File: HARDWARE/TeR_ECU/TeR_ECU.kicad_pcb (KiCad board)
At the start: 4 copper layers, 108.5 x 67.8 mm, 167 parts, among them IC1 MX34040NF2, J1 RJ45_Shielded, J2 RJ45_Shielded, J3 DEBUG, J4 USB_B_Mini, J5 GPS_ANT, K2 G5Q-1, Q1 ZXMN3F30FH, Q2 ZXMN3F30FH, Q3 ZXMN3F30FH, Q4 ZXMN3F30FH, Q5 ZXMN3F30FH, SW1 RST, SW2 BOOT0, U1 TCAN332, U10 NEO-M9N, U11 AT24CS02-STUM, U2 TCAN332, U3 TSR_1-2450, U4 LM1117MP-3.3, U5 LM324, U6 STM32F405VGTx, U7 USBLC6-2SC6, U8 ASM330LHH, U9 LIS3MDL, Y2 ECS-250-20-33-CKM-TR

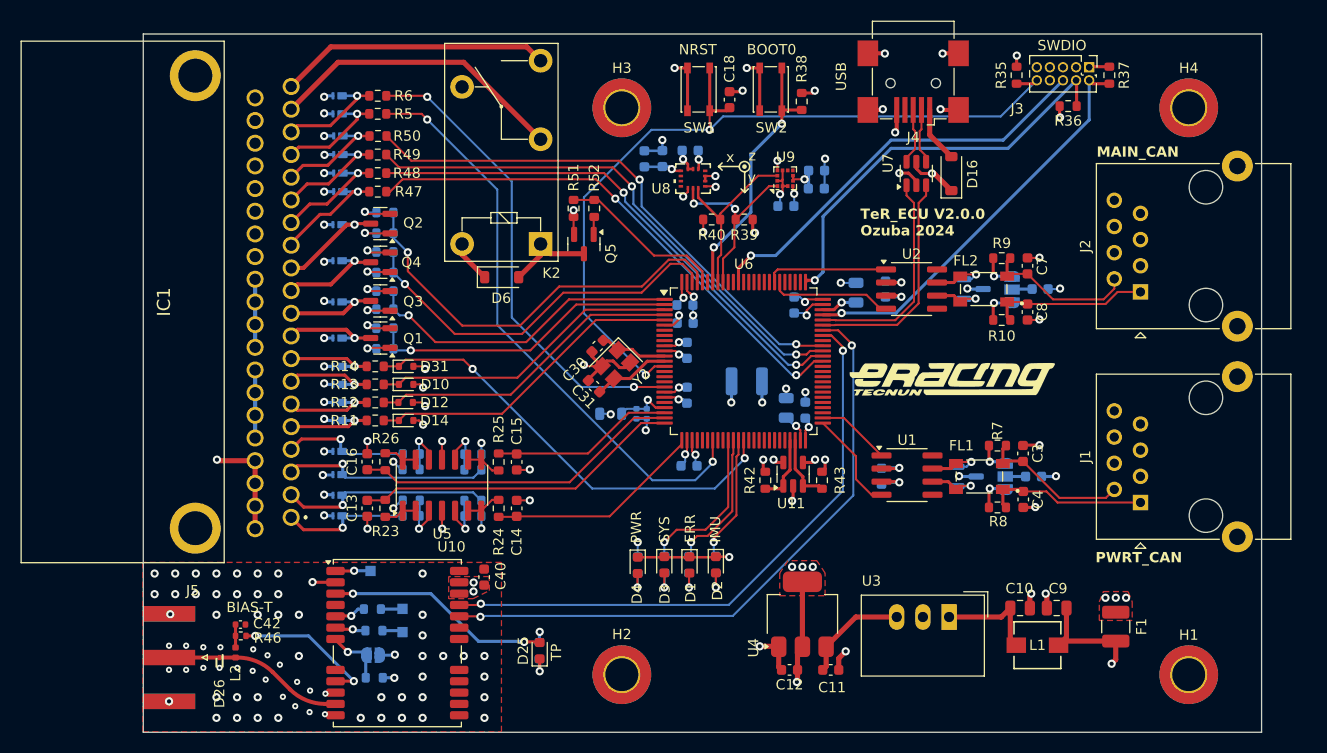
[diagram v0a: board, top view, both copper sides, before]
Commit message: Corregidos conectores, CAN y añadidas librerias al proyecto para cargar huellas
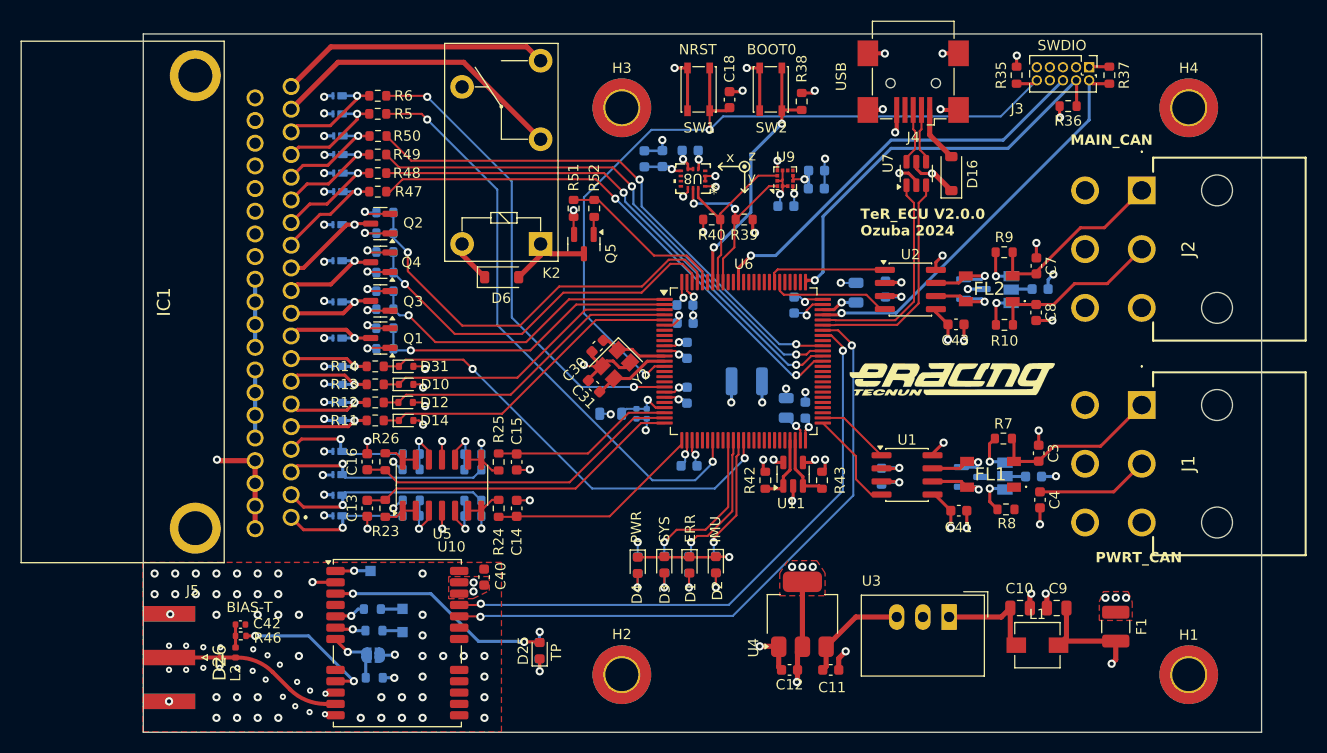
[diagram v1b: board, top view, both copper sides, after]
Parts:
- added C41: 100n, Capacitor_SMD:C_0603_1608Metric, F.Cu at (171.4, 104.8)
- added C43: 100n, Capacitor_SMD:C_0603_1608Metric, F.Cu at (171.1, 86.7)
- D26: footprint GPS_D:SODFL1006X40N -> ESD9101:SODFL1006X40N
- FL1, FL2: footprint CAN_CMF:FIL_ACT45B-510-2P-TL003 -> ACT45B-510-2P-TL003:ACT45B1012PTL003
- J1, J2: value RJ45_Shielded -> 76825-0006; footprint Connector_RJ:RJ45_Ninigi_GE -> 76825-0006:768250006
- JP1, JP2: value 120R Term -> SolderJumper_3_Open; footprint Jumper:SolderJumper-3_P1.3mm_Open_RoundedPad1.0x1.5mm -> Jumper:SolderJumper-3_P1.3mm_Open_Pad1.0x1.5mm
- L1: footprint footprints:IND_TCK-141_TRP -> Inductor_SMD:L_TracoPower_TCK-141
- U1, U2: value TCAN332 -> TCAN3403DR-Q1
- U8: footprint IMU:LGA-14L_2P5X3X0P83_STM-L -> ASM330:LGA-14L_2P5X3X0P83_STM-L
- moved J2 9.86 mm to (189.1, 73.7)
- moved J1 9.46 mm to (189.1, 94.5)
- moved C4 1.63 mm to (179.2, 103.7)
- moved C3 1.53 mm to (179.1, 99.2)
- moved FL1 1.10 mm to (174.4, 101.2)
- moved R7 0.89 mm to (175.7, 97.8)
- moved C7 0.86 mm to (178.9, 81.0)
- moved R8 0.85 mm to (175.9, 104.6)
- moved C8 0.84 mm to (178.9, 85.5)
- moved R9 0.62 mm to (175.8, 79.7)
- moved R10 0.54 mm to (175.8, 86.7)
- moved FL2 0.54 mm to (174.3, 83.2)
- moved D7 0.44 mm to (172.6, 101.5)
- moved U2 0.12 mm to (166.7, 83.3)
- moved JP2 0.09 mm to (176.4, 83.3)
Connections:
- J1 pad 1: /CAN_MAIN/CAN- -> /CAN_MAIN/CAN+
- J1 pad 2: /CAN_MAIN/CAN+ -> /CAN_MAIN/CAN-
- J1 pad 3: 24_VIN -> /LV_CAN/shield
- J1 pad 5: 24_VIN -> GND
- J1 pad 6: GND -> unconnected-(J1-Pad6)
- J2 pad 1: /CAN_POWERTRAIN/CAN- -> /CAN_POWERTRAIN/CAN+
- J2 pad 2: /CAN_POWERTRAIN/CAN+ -> /CAN_POWERTRAIN/CAN-
- J2 pad 3: 24_VIN -> /PowerTrain/shield
- J2 pad 5: 24_VIN -> GND
- J2 pad 6: GND -> unconnected-(J2-Pad6)
- U1 pad 5: unconnected-(U1-NC-Pad5) -> +3.3V
- U1 pad 8: unconnected-(U1-NC-Pad8) -> GND
- U2 pad 5: unconnected-(U2-NC-Pad5) -> +3.3V
- U2 pad 8: unconnected-(U2-NC-Pad8) -> GND
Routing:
- net +3.3V: track 82.6 -> 90.1 mm, vias 35 -> 37
- net GND: track 154.5 -> 161.1 mm, vias 149 -> 152
- net /CAN_MAIN/CAN-: track 15.8 -> 11.0 mm
- net /CAN_POWERTRAIN/CAN+: track 14.8 -> 18.4 mm
- net /CAN_MAIN/CAN+: track 14.9 -> 17.0 mm
- net Net-(U1-CANH): track 5.63 -> 7.65 mm
- net Net-(U2-CANL): track 5.28 -> 7.09 mm
- net /CAN_POWERTRAIN/CAN-: track 15.4 -> 17.1 mm
- net Net-(U2-CANH): track 5.51 -> 7.22 mm
- net Net-(U1-CANL): track 5.52 -> 6.62 mm
- net Net-(JP1-A): track 3.15 -> 4.03 mm
- net Net-(JP2-A): track 3.53 -> 4.09 mm

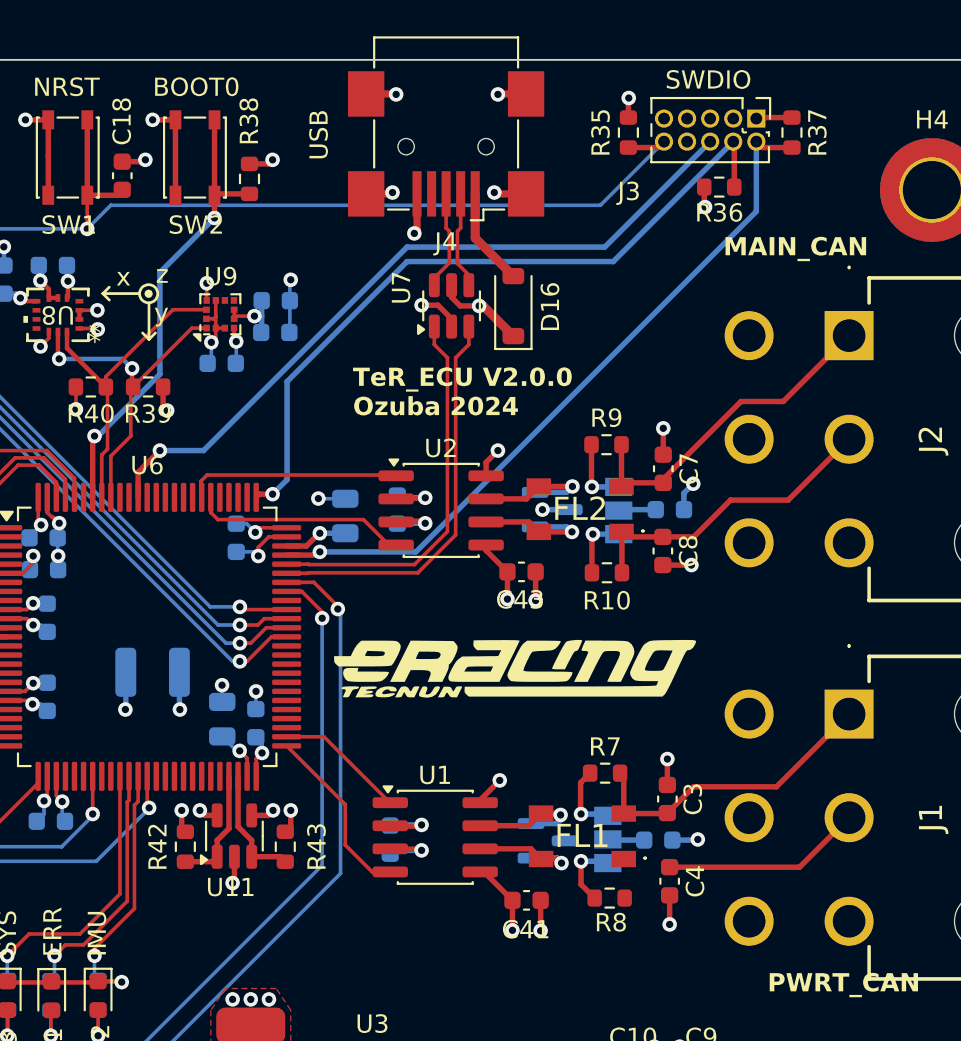
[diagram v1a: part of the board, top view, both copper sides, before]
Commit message: Arreglado plano 24_VIN y rutas CAN
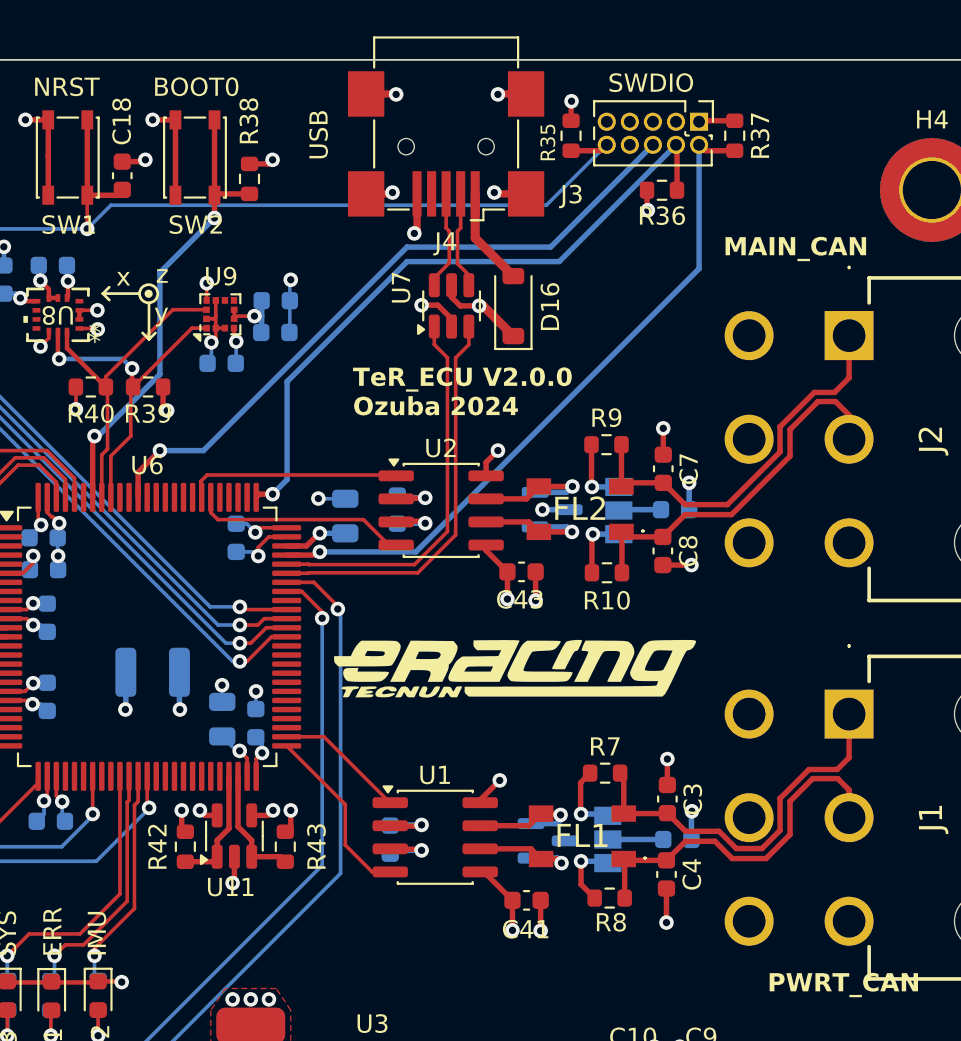
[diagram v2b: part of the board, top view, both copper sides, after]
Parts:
- moved R35 3.16 mm to (173.8, 62.7)
- moved J3 3.15 mm to (180.9, 61.9)
- moved R36 3.15 mm to (178.8, 65.7)
- moved R37 3.15 mm to (182.8, 62.7)
- moved C2 1.05 mm to (179.7, 101.4)
- moved C4 0.41 mm to (179.1, 103.3)
- moved C6 0.29 mm to (179.6, 83.2)
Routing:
- net /CAN_MAIN/CAN-: track 11.0 -> 20.1 mm
- net /CAN_POWERTRAIN/CAN+: track 18.4 -> 22.8 mm
- net /CAN_MAIN/CAN+: track 17.0 -> 21.0 mm
- net /MICRO_F4/NRST: track 80.7 -> 77.0 mm
- net /CAN_POWERTRAIN/CAN-: track 17.1 -> 20.5 mm
- net /MICRO_F4/SWCLK: track 40.0 -> 36.7 mm
- net /MICRO_F4/SWO: track 40.4 -> 37.2 mm
- net /MICRO_F4/SWDIO: track 39.6 -> 37.7 mm
- net Net-(JP1-C): track 1.97 -> 3.05 mm

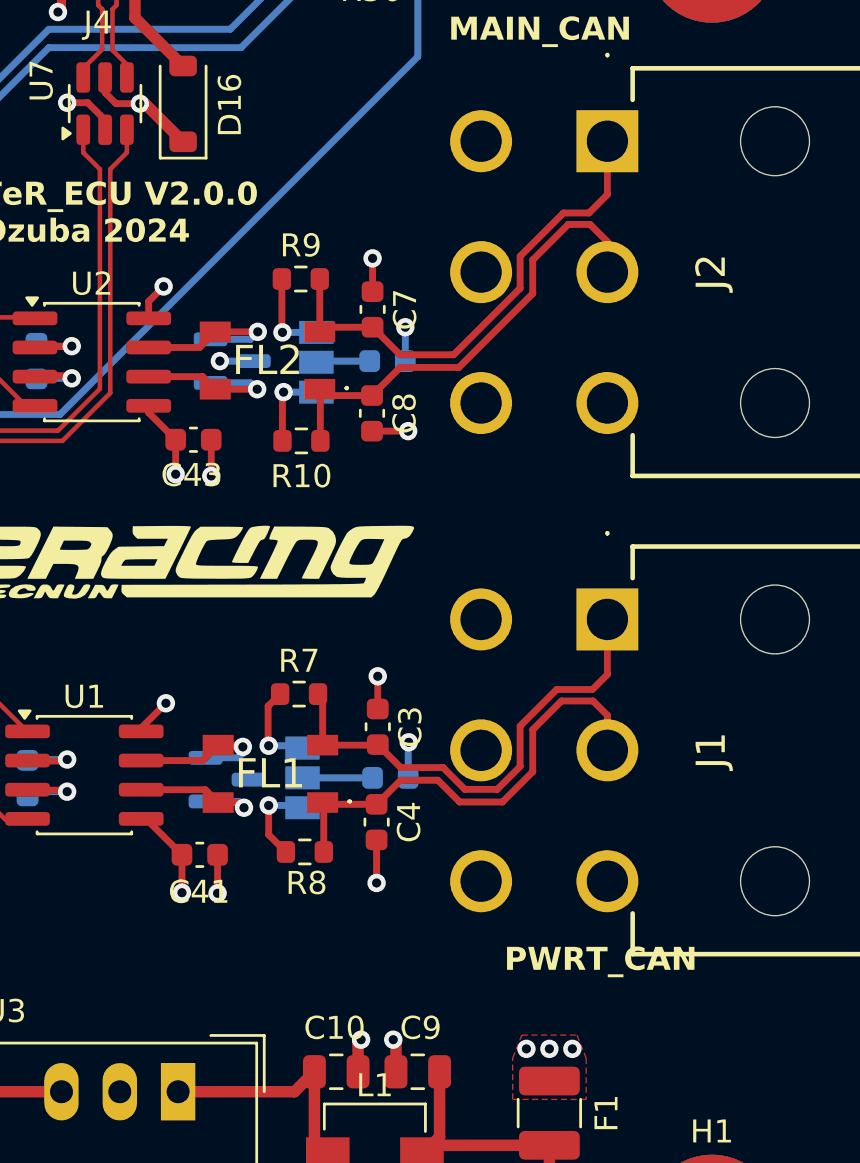
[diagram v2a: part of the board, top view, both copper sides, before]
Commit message: Arreglados tracks CAN (otra vez)
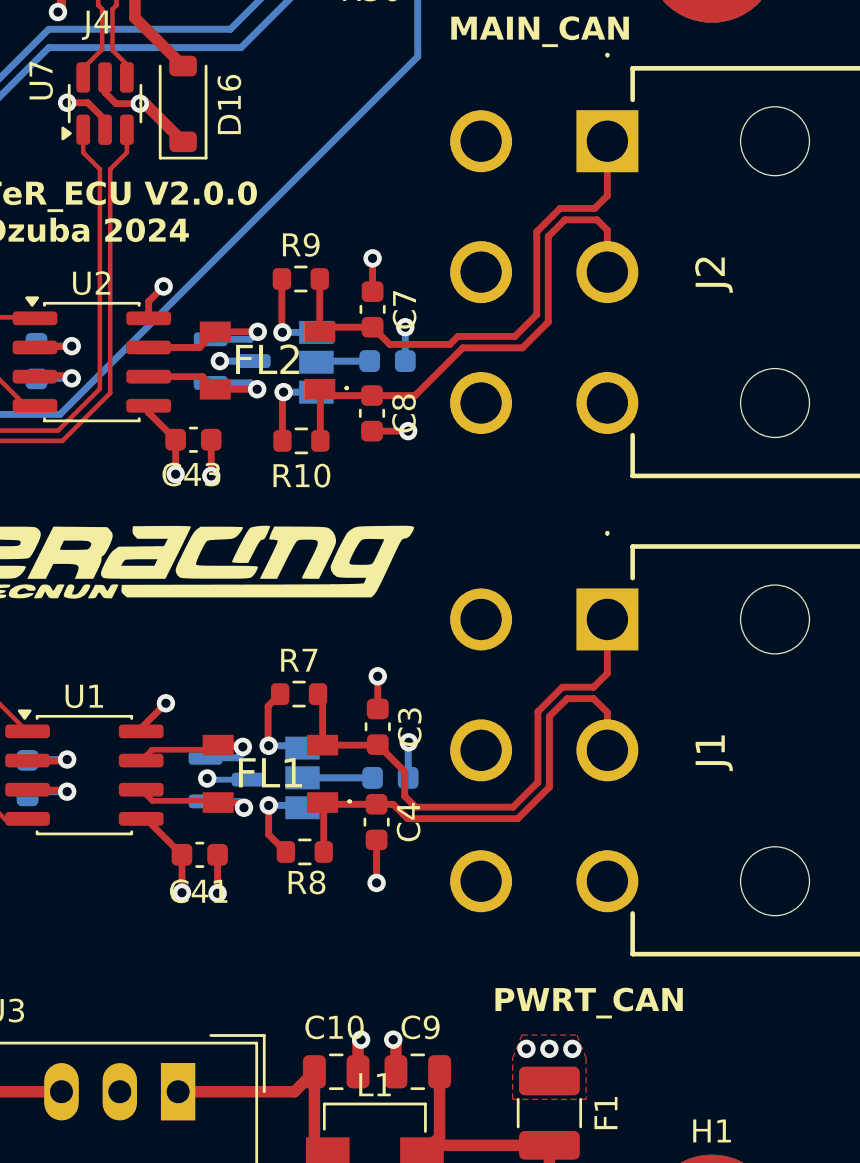
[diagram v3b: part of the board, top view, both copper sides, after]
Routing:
- net /CAN_MAIN/CAN+: track 21.0 -> 23.0 mm
- net GND: track 161.3 -> 163.1 mm, vias 152 -> 153
- net /CAN_POWERTRAIN/CAN-: track 20.5 -> 22.3 mm
- net /CAN_POWERTRAIN/CAN+: track 22.8 -> 23.8 mm
- net /CAN_MAIN/CAN-: track 20.1 -> 20.7 mm
